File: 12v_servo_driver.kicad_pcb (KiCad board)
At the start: 2 copper layers, 36.4 x 15 mm, 7 parts, among them J1 PWR/Signal, J2 Servo, U1 AMS1117-5.0

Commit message: Update page info and add gerber
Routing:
- net Net-(C1-Pad1): track 25.4 -> 24.7 mm
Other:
- board text added: "https://github.com/ theworkisthework/ 12v_servo_driver_module"
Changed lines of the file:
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@@
   (general
     (thickness 1.6)
-    (drawings 31)
+    (drawings 32)
     (tracks 21)
     (zones 0)
@@
   )
   (page A4)
+  (title_block
+    (title "12v Servo driver module")
+    (date 2022-09-19)
+    (rev A)
+    (company theworkisthework)
+  )
   (layers
     (0 F.Cu signal)
@@
     (36 B.SilkS user)
     (37 F.SilkS user)
-    (38 B.Mask user)
-    (39 F.Mask user)
-    (40 Dwgs.User user)
-    (41 Cmts.User user)
+    (38 B.Mask user hide)
+    (39 F.Mask user hide)
+    (40 Dwgs.User user hide)
+    (41 Cmts.User user hide)
     (42 Eco1.User user hide)
     (43 Eco2.User user hide)
-    (44 Edge.Cuts user)
+    (44 Edge.Cuts user hide)
     (45 Margin user hide)
     (46 B.CrtYd user hide)
@@
   )
   (setup
-    (last_trace_width 0.25)
+    (last_trace_width 0.75)
     (user_trace_width 0.35)
     (user_trace_width 0.4)
@@
       (effects (font (size 0.88 0.88) (thickness 0.13)))
     )
-    (pad 2 smd roundrect (at 1.5375 0 180) (size 1.325 2.35) (layers F.Cu F.Paste F.Mask) (roundrect_rratio 0.188679)
+    (pad 2 smd roundrect (at 1.5375 0 180) (size 1.325 2.35) (layers F.Cu F.Paste F.Mask) (roundrect_rratio 0.1886784905660377)
       (net 2 GND))
-    (pad 1 smd roundrect (at -1.5375 0 180) (size 1.325 2.35) (layers F.Cu F.Paste F.Mask) (roundrect_rratio 0.188679)
+    (pad 1 smd roundrect (at -1.5375 0 180) (size 1.325 2.35) (layers F.Cu F.Paste F.Mask) (roundrect_rratio 0.1886784905660377)
       (net 3 "Net-(C2-Pad1)"))
     (model ${KISYS3DMOD}/Capacitor_Tantalum_SMD.3dshapes/CP_EIA-3528-21_Kemet-B.wrl
@@
       (effects (font (size 0.88 0.88) (thickness 0.13)))
     )
-    (pad 1 smd roundrect (at -1.5375 0 90) (size 1.325 2.35) (layers F.Cu F.Paste F.Mask) (roundrect_rratio 0.188679)
+    (pad 1 smd roundrect (at -1.5375 0 90) (size 1.325 2.35) (layers F.Cu F.Paste F.Mask) (roundrect_rratio 0.1886784905660377)
       (net 1 "Net-(C1-Pad1)"))
-    (pad 2 smd roundrect (at 1.5375 0 90) (size 1.325 2.35) (layers F.Cu F.Paste F.Mask) (roundrect_rratio 0.188679)
+    (pad 2 smd roundrect (at 1.5375 0 90) (size 1.325 2.35) (layers F.Cu F.Paste F.Mask) (roundrect_rratio 0.1886784905660377)
       (net 2 GND))
     (model ${KISYS3DMOD}/Capacitor_Tantalum_SMD.3dshapes/CP_EIA-3528-21_Kemet-B.wrl
@@
       (effects (font (size 1 1) (thickness 0.15)))
     )
-    (pad 1 thru_hole roundrect (at 0 0 270) (size 1.2 1.75) (drill 0.75) (layers *.Cu *.Mask) (roundrect_rratio 0.208333)
+    (pad 1 thru_hole roundrect (at 0 0 270) (size 1.2 1.75) (drill 0.75) (layers *.Cu *.Mask) (roundrect_rratio 0.2083325)
       (net 4 /PWM))
     (pad 2 thru_hole oval (at 2 0 270) (size 1.2 1.75) (drill 0.75) (layers *.Cu *.Mask)
@@
       (rotate (xyz 0 0 0))
     )
+  )
+  (gr_text "https://github.com/\ntheworkisthework/\n12v_servo_driver_module" (at 152.2603 108.5596) (layer B.SilkS)
+    (effects (font (size 1 1) (thickness 0.15)) (justify mirror))
   )
   (gr_text Servo (at 150.0124 106.7689 90) (layer F.SilkS)
@@
   (gr_arc (start 162.6489 117.6147) (end 162.6489 118.6053) (angle -90) (layer Edge.Cuts) (width 0.05))
   (gr_line (start 162.1917 118.6053) (end 162.6489 118.6053) (layer Edge.Cuts) (width 0.05))
-  (gr_text "Rev: A Servo Controller" (at 153.162 117.1702) (layer B.SilkS)
+  (gr_text "Rev: A Servo Controller" (at 151.9555 105.2068) (layer B.SilkS)
     (effects (font (size 1 1) (thickness 0.15)) (justify mirror))
   )
@@
   (segment (start 162.67651 112.997834) (end 162.67651 109.79451) (width 0.75) (layer F.Cu) (net 1))
   (segment (start 161.2265 114.3061) (end 161.368244 114.3061) (width 0.75) (layer F.Cu) (net 1))
-  (segment (start 148.0579 111.9386) (end 148.0579 114.949) (width 0.75) (layer F.Cu) (net 1))
-  (segment (start 148.0579 114.949) (end 150.1267 117.0178) (width 0.75) (layer F.Cu) (net 1))
-  (segment (start 150.1267 117.0178) (end 157.4038 117.0178) (width 0.75) (layer F.Cu) (net 1))
-  (segment (start 160.1155 114.3061) (end 161.2265 114.3061) (width 0.75) (layer F.Cu) (net 1))
-  (segment (start 157.4038 117.0178) (end 160.1155 114.3061) (width 0.75) (layer F.Cu) (net 1))
+  (segment (start 148.0579 114.949) (end 148.0579 111.9386) (width 0.75) (layer F.Cu) (net 1))
+  (segment (start 149.2758 116.1669) (end 148.0579 114.949) (width 0.75) (layer F.Cu) (net 1))
+  (segment (start 159.3469 116.1669) (end 149.2758 116.1669) (width 0.75) (layer F.Cu) (net 1))
+  (segment (start 161.2077 114.3061) (end 159.3469 116.1669) (width 0.75) (layer F.Cu) (net 1))
+  (segment (start 161.2265 114.3061) (end 161.2077 114.3061) (width 0.75) (layer F.Cu) (net 1))
   (segment (start 143.256 115.5192) (end 143.637 115.1382) (width 0.75) (layer F.Cu) (net 2))
   (segment (start 143.637 112.1177) (end 143.4579 111.9386) (width 0.75) (layer F.Cu) (net 2))

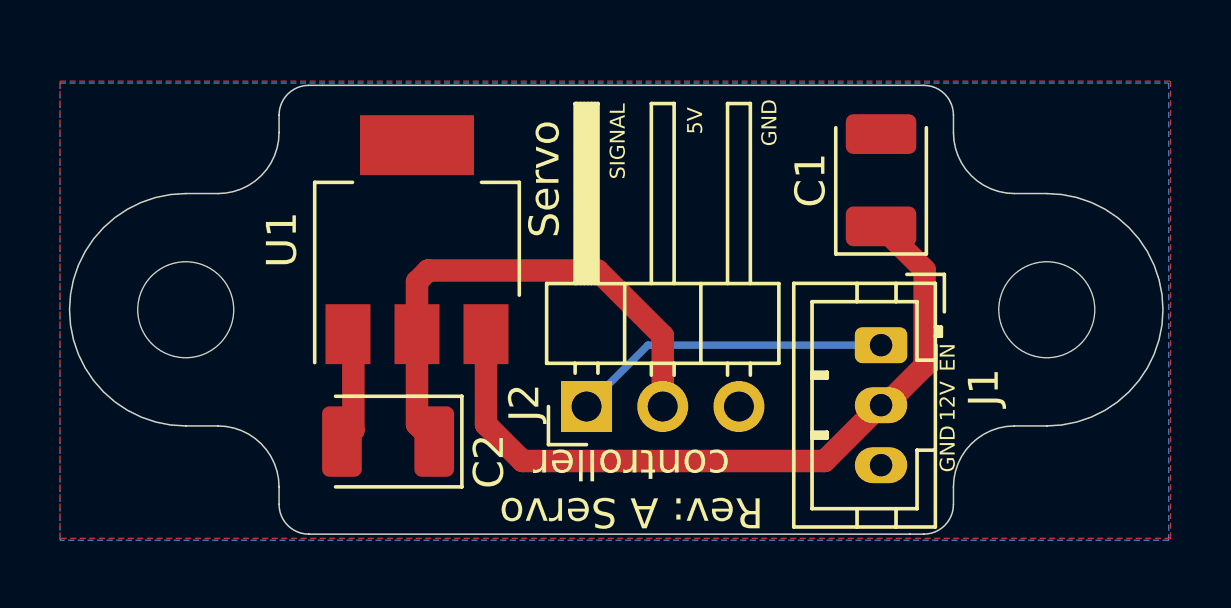
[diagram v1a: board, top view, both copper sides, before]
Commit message: Add pinout documentation
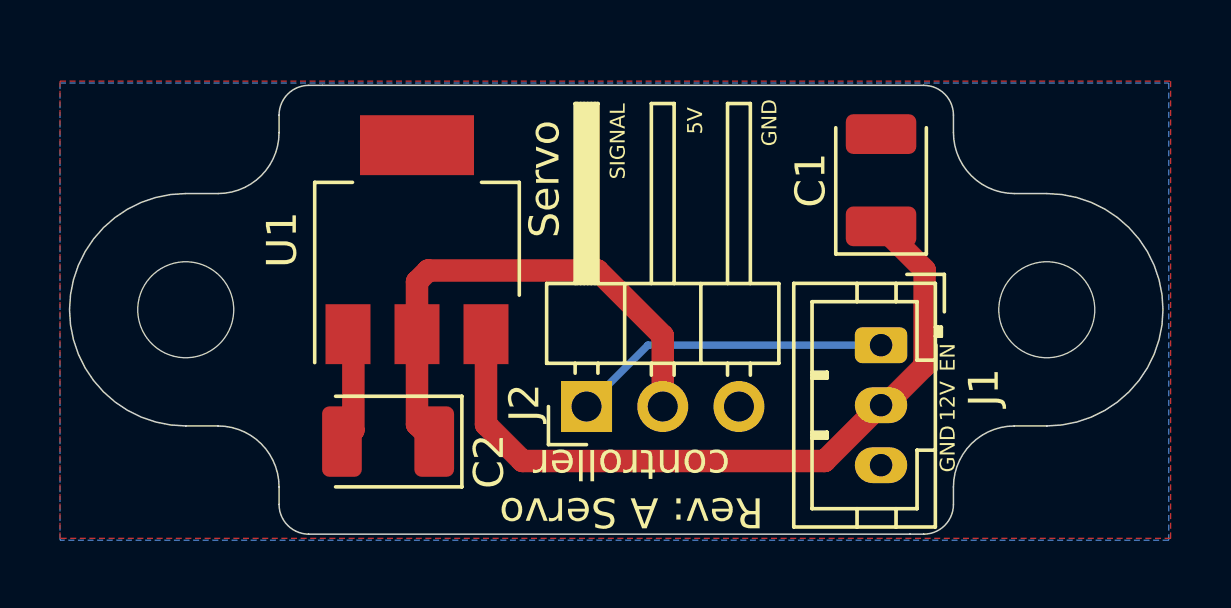
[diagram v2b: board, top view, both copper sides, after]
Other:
- net class Default removed
- board text added: "~{EN}"
- board text removed: "~EN"

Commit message: RevB
Right angle connectors on both servo and controller connectors.
Both connectors on same side of the board.
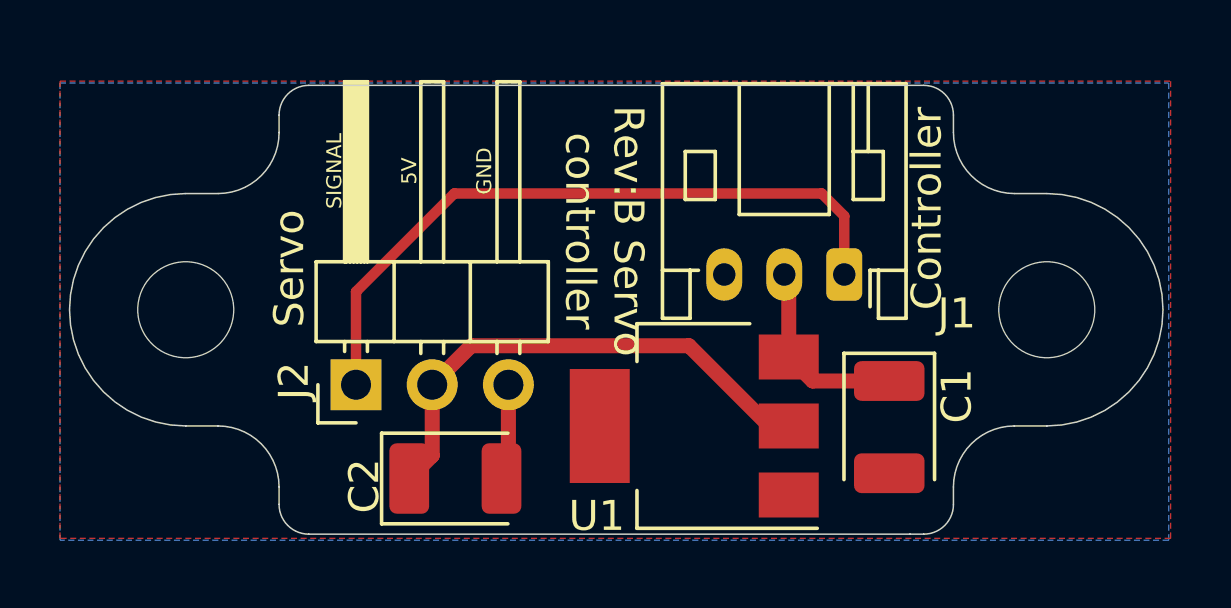
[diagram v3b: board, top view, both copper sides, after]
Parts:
- J1: footprint Connector_JST:JST_PH_B3B-PH-K_1x03_P2.00mm_Vertical -> Connector_JST:JST_PH_S3B-PH-K_1x03_P2.00mm_Horizontal
- moved U1 11.1 mm to (155.0, 115.0), turned to 180 degrees
- moved C1 8.24 mm to (161.5, 115.0), turned to -90 degrees
- moved J2 7.72 mm to (143.7, 113.6)
- moved J1 2.66 mm to (160.0, 110.0), turned to 180 degrees
- moved C2 2.56 mm to (147.0, 116.8), turned to 0 degrees
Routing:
- net Net-(J1-Pin_2): track 24.7 -> 6.49 mm
- net /PWM: track 10.7 -> 23.0 mm
- net GND: track 3.81 -> 3.22 mm
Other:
- board text added: "Controller"
- board text added: "Rev:B Servo controller"
- board text removed: "12V"
- board text removed: "Rev: A Servo controller"
- board text removed: "~{EN}"
